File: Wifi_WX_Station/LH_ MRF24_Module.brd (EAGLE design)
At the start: 23.2 x 32.4 mm, 7 parts, among them M1 MRF24WB0MA

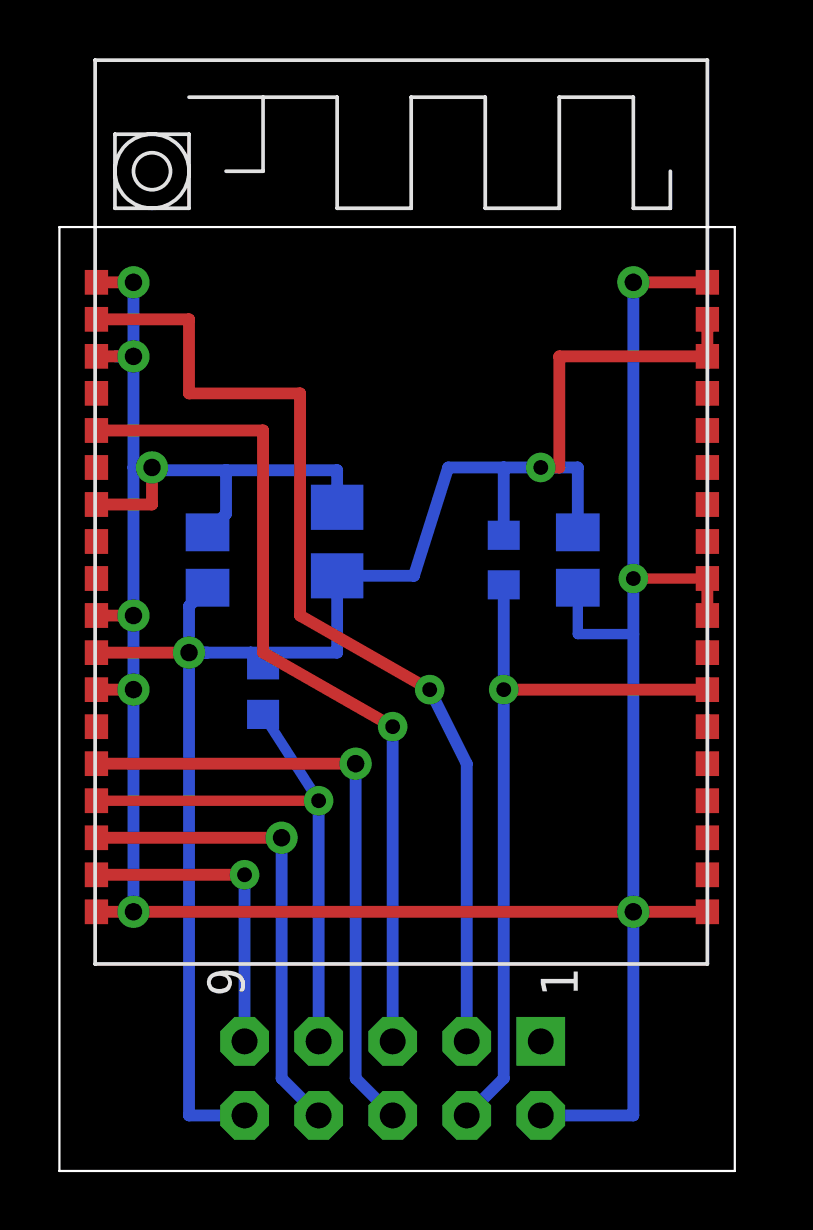
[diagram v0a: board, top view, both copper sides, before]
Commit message: added SILabs Hygrometer board Added frames to the schematics
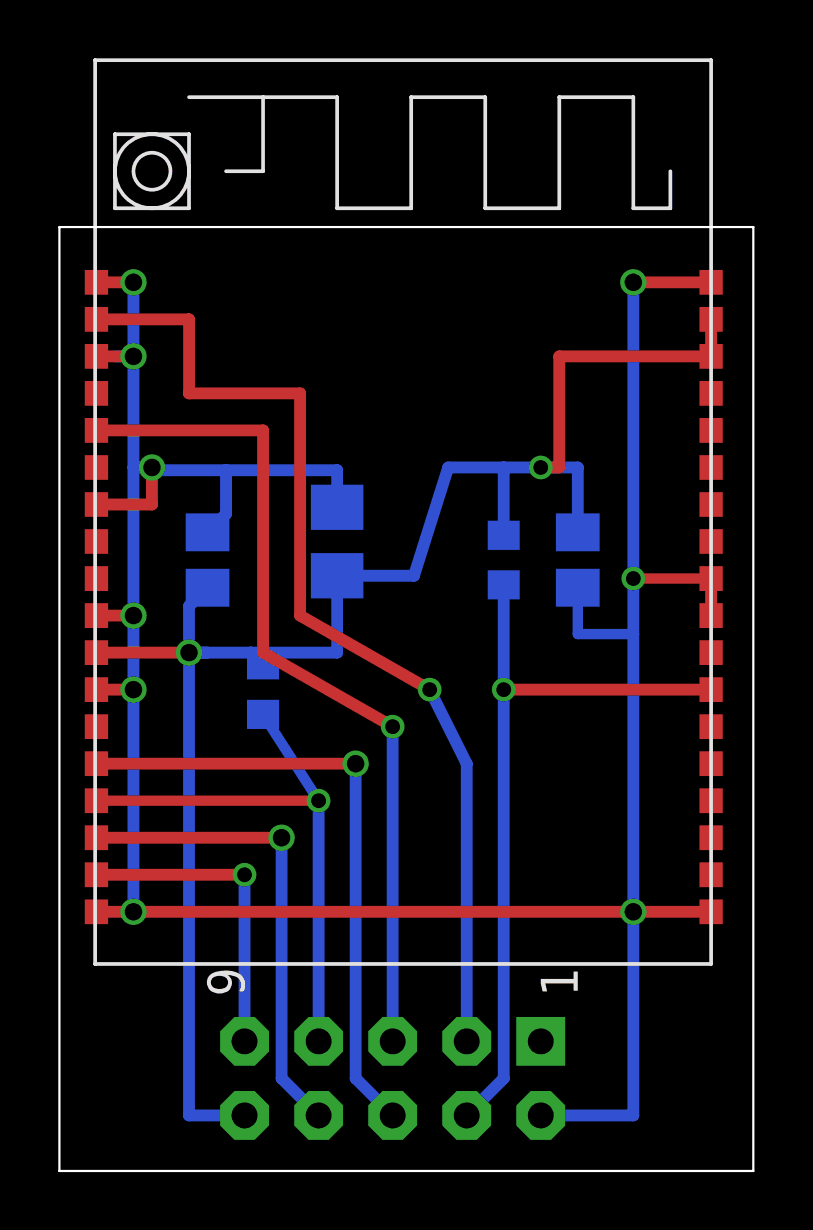
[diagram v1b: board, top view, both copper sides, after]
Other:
- board size 23.2 x 32.4 mm -> 23.8 x 32.4 mm
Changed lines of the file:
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@@
 <setting verticaltext="up"/>
 </settings>
-<grid distance="0.05" unitdist="inch" unit="inch" style="lines" multiple="1" display="no" altdistance="0.025" altunitdist="inch" altunit="inch"/>
+<grid distance="0.05" unitdist="inch" unit="inch" style="lines" multiple="1" display="yes" altdistance="0.025" altunitdist="inch" altunit="inch"/>
 <layers>
 <layer number="1" name="Top" color="4" fill="1" visible="yes" active="yes"/>
@@
 <layer number="35" name="tGlue" color="7" fill="4" visible="yes" active="yes"/>
 <layer number="36" name="bGlue" color="7" fill="5" visible="yes" active="yes"/>
+<layer number="37" name="tTest" color="7" fill="1" visible="yes" active="yes"/>
+<layer number="38" name="bTest" color="7" fill="1" visible="yes" active="yes"/>
 <layer number="39" name="tKeepout" color="4" fill="11" visible="yes" active="yes"/>
 <layer number="40" name="bKeepout" color="1" fill="11" visible="yes" active="yes"/>
@@
 <layer number="97" name="Info" color="7" fill="1" visible="no" active="no"/>
 <layer number="98" name="Guide" color="6" fill="1" visible="no" active="no"/>
+<layer number="100" name="Moduls" color="14" fill="0" visible="yes" active="yes"/>
+<layer number="101" name="Flex-Kleb" color="1" fill="7" visible="yes" active="yes"/>
 <layer number="104" name="Name" color="16" fill="1" visible="yes" active="yes"/>
+<layer number="105" name="Beschreib" color="9" fill="1" visible="yes" active="yes"/>
+<layer number="106" name="BGA-Top" color="4" fill="1" visible="yes" active="yes"/>
+<layer number="107" name="BD-Top" color="5" fill="1" visible="yes" active="yes"/>
 <layer number="116" name="Patch_BOT" color="9" fill="4" visible="yes" active="yes"/>
 <layer number="121" name="_tsilk" color="7" fill="1" visible="yes" active="yes"/>
 <layer number="122" name="_bsilk" color="7" fill="1" visible="yes" active="yes"/>
 <layer number="125" name="_tNames" color="7" fill="1" visible="yes" active="yes"/>
-<layer number="144" name="Drill_legend" color="7" fill="1" visible="yes" active="yes"/>
+<layer number="144" name="Drill_legend" color="7" fill="1" visible="no" active="yes"/>
 <layer number="151" name="HeatSink" color="7" fill="1" visible="yes" active="yes"/>
 <layer number="200" name="200bmp" color="1" fill="10" visible="no" active="no"/>
@@
 <board>
 <plain>
-<wire x1="20.955" y1="27.94" x2="44.12" y2="27.94" width="0.0762" layer="20"/>
-<wire x1="44.12" y1="27.94" x2="44.12" y2="60.315" width="0.0762" layer="20"/>
-<wire x1="44.12" y1="60.315" x2="20.955" y2="60.315" width="0.0762" layer="20"/>
+<wire x1="20.955" y1="27.94" x2="44.755" y2="27.94" width="0.0762" layer="20"/>
+<wire x1="44.755" y1="27.94" x2="44.755" y2="60.315" width="0.0762" layer="20"/>
+<wire x1="44.755" y1="60.315" x2="20.955" y2="60.315" width="0.0762" layer="20"/>
 <wire x1="20.955" y1="60.315" x2="20.955" y2="27.94" width="0.0762" layer="20"/>
 <text x="43.18" y="58.42" size="1.4224" layer="26" font="vector" rot="MR270">RV Builders Product 2013</text>
@@
 </class>
 </classes>
-<designrules name="sparkfun">
-<description language="en">&lt;b&gt;SPARKFUN Design Rules&lt;/b&gt;
+<designrules name="Elecrow_2-layer_with reduced cream mask">
+<description language="de">&lt;b&gt;EAGLE Design Rules&lt;/b&gt;
 &lt;p&gt;
-The Sparkfun Design Rules have been set to cover
-a wide range of applications. Your particular design
-may have different requirements, so please make the
-necessary adjustments and save your customized
-design rules under a new name.</description>
+Die Standard-Design-Rules sind so gewählt, dass sie für
+die meisten Anwendungen passen. Sollte ihre Platine
+besondere Anforderungen haben, treffen Sie die erforderlichen
+Einstellungen hier und speichern die Design Rules unter
+einem neuen Namen ab.</description>
+<description language="en">&lt;b&gt;ELCROW rules&lt;/b&gt;
+</description>
+<description language="zh">&lt;b&gt;Elecrow EAGLE Design Rules&lt;/b&gt;
+</description>
 <param name="layerSetup" value="(1*16)"/>
 <param name="mtCopper" value="0.035mm 0.035mm 0.035mm 0.035mm 0.035mm 0.035mm 0.035mm 0.035mm 0.035mm 0.035mm 0.035mm 0.035mm 0.035mm 0.035mm 0.035mm 0.035mm"/>
 <param name="mtIsolate" value="1.5mm 0.15mm 0.2mm 0.15mm 0.2mm 0.15mm 0.2mm 0.15mm 0.2mm 0.15mm 0.2mm 0.15mm 0.2mm 0.15mm 0.2mm"/>
-<param name="mdWireWire" value="8mil"/>
-<param name="mdWirePad" value="8mil"/>
-<param name="mdWireVia" value="8mil"/>
-<param name="mdPadPad" value="8mil"/>
-<param name="mdPadVia" value="8mil"/>
-<param name="mdViaVia" value="8mil"/>
-<param name="mdSmdPad" value="8mil"/>
-<param name="mdSmdVia" value="8mil"/>
-<param name="mdSmdSmd" value="8mil"/>
+<param name="mdWireWire" value="6mil"/>
+<param name="mdWirePad" value="6mil"/>
+<param name="mdWireVia" value="6mil"/>
+<param name="mdPadPad" value="6mil"/>
+<param name="mdPadVia" value="6mil"/>
+<param name="mdViaVia" value="6mil"/>
+<param name="mdSmdPad" value="0mil"/>
+<param name="mdSmdVia" value="0mil"/>
+<param name="mdSmdSmd" value="0mil"/>
 <param name="mdViaViaSameLayer" value="8mil"/>
 <param name="mnLayersViaInSmd" value="2"/>
 <param name="mdCopperDimension" value="10mil"/>
-<param name="mdDrill" value="8mil"/>
+<param name="mdDrill" value="10mil"/>
 <param name="mdSmdStop" value="0mil"/>
-<param name="msWidth" value="8mil"/>
-<param name="msDrill" value="20mil"/>
-<param name="msMicroVia" value="9.99mm"/>
+<param name="msWidth" value="6mil"/>
+<param name="msDrill" value="12mil"/>
+<param name="msMicroVia" value="12mil"/>
 <param name="msBlindViaRatio" value="0.5"/>
 <param name="rvPadTop" value="0.25"/>
@@
 <param name="rvMicroViaOuter" value="0.25"/>
 <param name="rvMicroViaInner" value="0.25"/>
-<param name="rlMinPadTop" value="12mil"/>
+<param name="rlMinPadTop" value="10mil"/>
 <param name="rlMaxPadTop" value="20mil"/>
 <param name="rlMinPadInner" value="10mil"/>
 <param name="rlMaxPadInner" value="20mil"/>
-<param name="rlMinPadBottom" value="12mil"/>
+<param name="rlMinPadBottom" value="10mil"/>
 <param name="rlMaxPadBottom" value="20mil"/>
-<param name="rlMinViaOuter" value="10mil"/>
+<param name="rlMinViaOuter" value="6mil"/>
 <param name="rlMaxViaOuter" value="20mil"/>
-<param name="rlMinViaInner" value="10mil"/>
+<param name="rlMinViaInner" value="6mil"/>
 <param name="rlMaxViaInner" value="20mil"/>
 <param name="rlMinMicroViaOuter" value="4mil"/>
@@
 <param name="psTop" value="-1"/>
 <param name="psBottom" value="-1"/>
-<param name="psFirst" value="-1"/>
+<param name="psFirst" value="0"/>
 <param name="psElongationLong" value="100"/>
 <param name="psElongationOffset" value="100"/>
 <param name="mvStopFrame" value="1"/>
-<param name="mvCreamFrame" value="0"/>
-<param name="mlMinStopFrame" value="4mil"/>
-<param name="mlMaxStopFrame" value="4mil"/>
-<param name="mlMinCreamFrame" value="0mil"/>
-<param name="mlMaxCreamFrame" value="0mil"/>
-<param name="mlViaStopLimit" value="25mil"/>
+<param name="mvCreamFrame" value="1"/>
+<param name="mlMinStopFrame" value="2mil"/>
+<param name="mlMaxStopFrame" value="2mil"/>
+<param name="mlMinCreamFrame" value="2mil"/>
+<param name="mlMaxCreamFrame" value="2mil"/>
+<param name="mlViaStopLimit" value="100mil"/>
 <param name="srRoundness" value="0"/>
 <param name="srMinRoundness" value="0mil"/>
@@
 <param name="checkAngle" value="0"/>
 <param name="checkFont" value="1"/>
-<param name="checkRestrict" value="1"/>
+<param name="checkRestrict" value="0"/>
 <param name="useDiameter" value="13"/>
 <param name="maxErrors" value="50"/>
@@
 <contactref element="JP1" pad="2"/>
 <contactref element="M1" pad="21"/>
-<wire x1="43.18" y1="48.26" x2="43.18" y2="46.99" width="0.4064" layer="1"/>
+<wire x1="43.307" y1="48.26" x2="43.307" y2="46.99" width="0.4064" layer="1"/>
 <wire x1="22.225" y1="50.8" x2="24.13" y2="50.8" width="0.4064" layer="1"/>
 <wire x1="24.13" y1="50.8" x2="24.13" y2="52.07" width="0.4064" layer="1"/>
 <via x="24.13" y="52.07" extent="1-16" drill="0.6"/>
 <wire x1="23.495" y1="36.83" x2="40.64" y2="36.83" width="0.4064" layer="1"/>
-<wire x1="43.18" y1="48.26" x2="40.64" y2="48.26" width="0.3556" layer="1"/>
+<wire x1="43.307" y1="48.26" x2="40.64" y2="48.26" width="0.3556" layer="1"/>
 <via x="40.64" y="48.26" extent="1-16" drill="0.508"/>
 <wire x1="40.64" y1="46.355" x2="38.735" y2="46.355" width="0.3556" layer="16"/>
 <wire x1="38.735" y1="46.355" x2="38.735" y2="47.945" width="0.3556" layer="16"/>
-<wire x1="43.18" y1="58.42" x2="40.64" y2="58.42" width="0.4064" layer="1"/>
+<wire x1="43.307" y1="58.42" x2="40.64" y2="58.42" width="0.4064" layer="1"/>
 <via x="40.64" y="58.42" extent="1-16" drill="0.6"/>
 <wire x1="40.64" y1="58.42" x2="40.64" y2="48.26" width="0.4064" layer="16"/>
-<wire x1="43.18" y1="36.83" x2="40.64" y2="36.83" width="0.4064" layer="1"/>
+<wire x1="43.307" y1="36.83" x2="40.64" y2="36.83" width="0.4064" layer="1"/>
 <via x="40.64" y="36.83" extent="1-16" drill="0.6"/>
 <wire x1="40.64" y1="36.83" x2="40.64" y2="46.355" width="0.4064" layer="16"/>
@@
 <wire x1="37.465" y1="52.07" x2="38.1" y2="52.07" width="0.4064" layer="1"/>
 <wire x1="38.1" y1="52.07" x2="38.1" y2="55.88" width="0.4064" layer="1"/>
-<wire x1="38.1" y1="55.88" x2="43.18" y2="55.88" width="0.4064" layer="1"/>
-<wire x1="43.18" y1="55.88" x2="43.18" y2="57.15" width="0.4064" layer="1"/>
+<wire x1="38.1" y1="55.88" x2="43.307" y2="55.88" width="0.4064" layer="1"/>
+<wire x1="43.307" y1="55.88" x2="43.307" y2="57.15" width="0.4064" layer="1"/>
 <via x="37.465" y="52.07" extent="1-16" drill="0.508"/>
 <wire x1="27.94" y1="45.3" x2="27.52" y2="45.72" width="0.4064" layer="16"/>
@@
 <contactref element="JP1" pad="4"/>
 <via x="36.195" y="44.45" extent="1-16" drill="0.508"/>
-<wire x1="43.18" y1="44.45" x2="36.195" y2="44.45" width="0.4064" layer="1"/>
+<wire x1="43.307" y1="44.45" x2="36.195" y2="44.45" width="0.4064" layer="1"/>
 <wire x1="36.195" y1="48.045" x2="36.195" y2="44.45" width="0.4064" layer="16"/>
 <wire x1="34.925" y1="29.845" x2="36.195" y2="31.115" width="0.4064" layer="16"/>
